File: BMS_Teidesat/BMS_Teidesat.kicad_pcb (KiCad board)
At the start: 2 copper layers, 90.2 x 95.9 mm, 10 parts

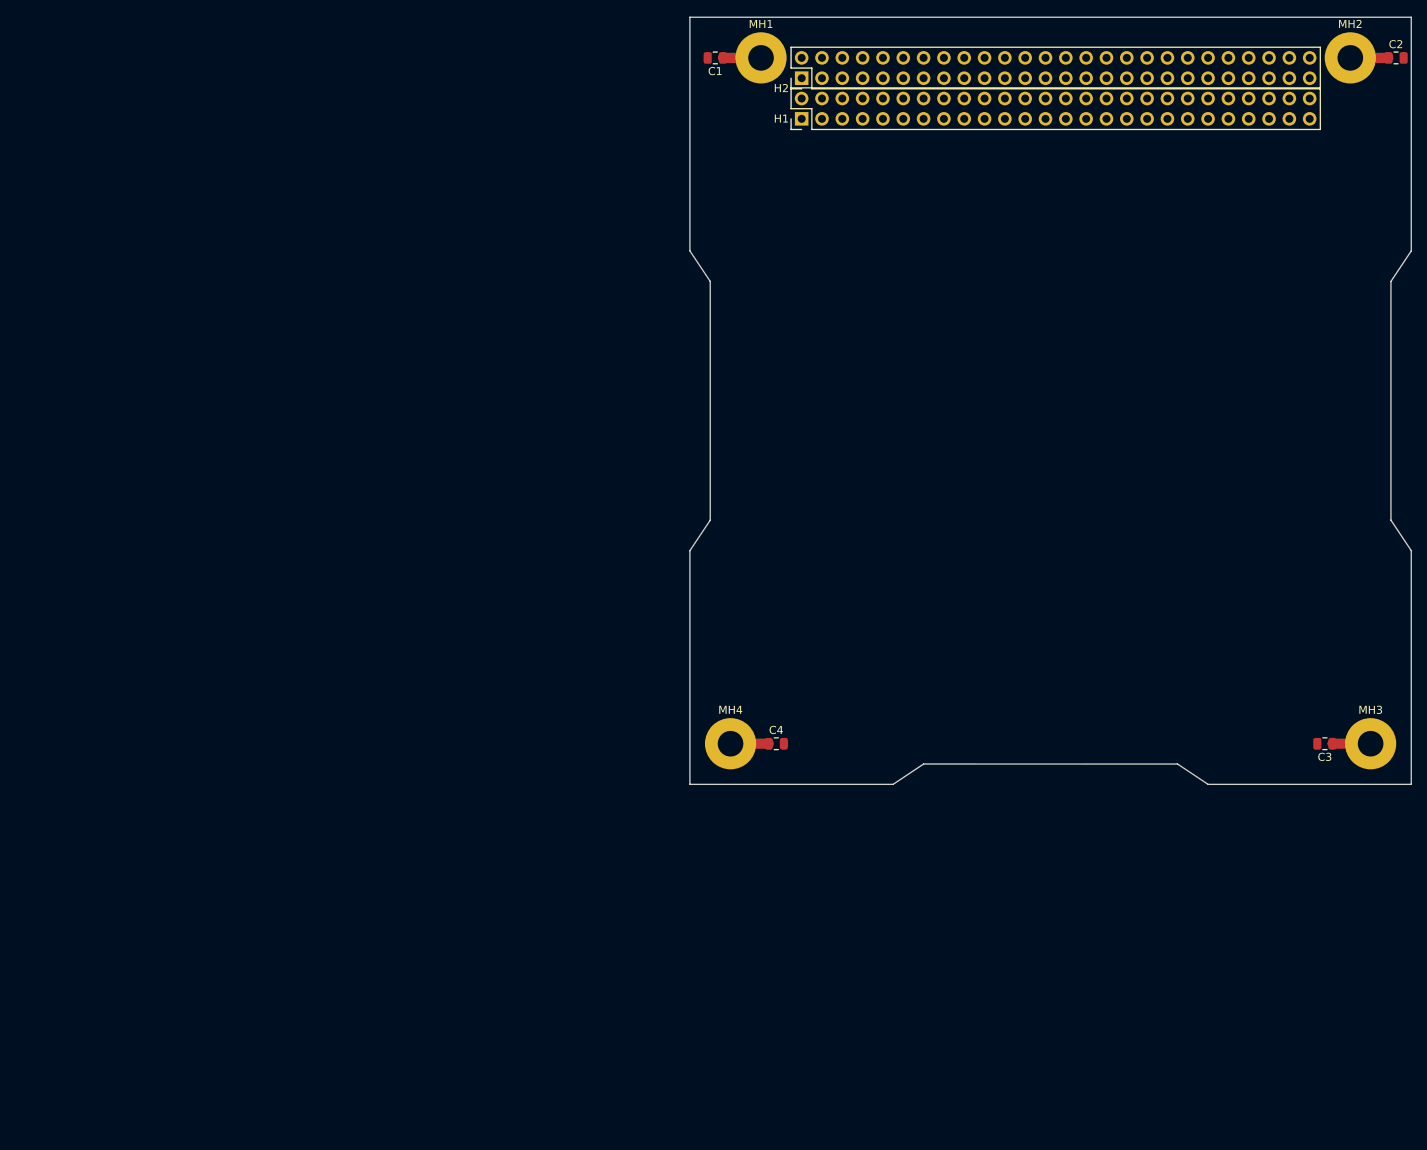
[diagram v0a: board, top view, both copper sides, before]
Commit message: Comienzo de enrutado
Co-Authored-By: hugohdezmo <238262256+hugohdezmo@users.noreply.github.com>
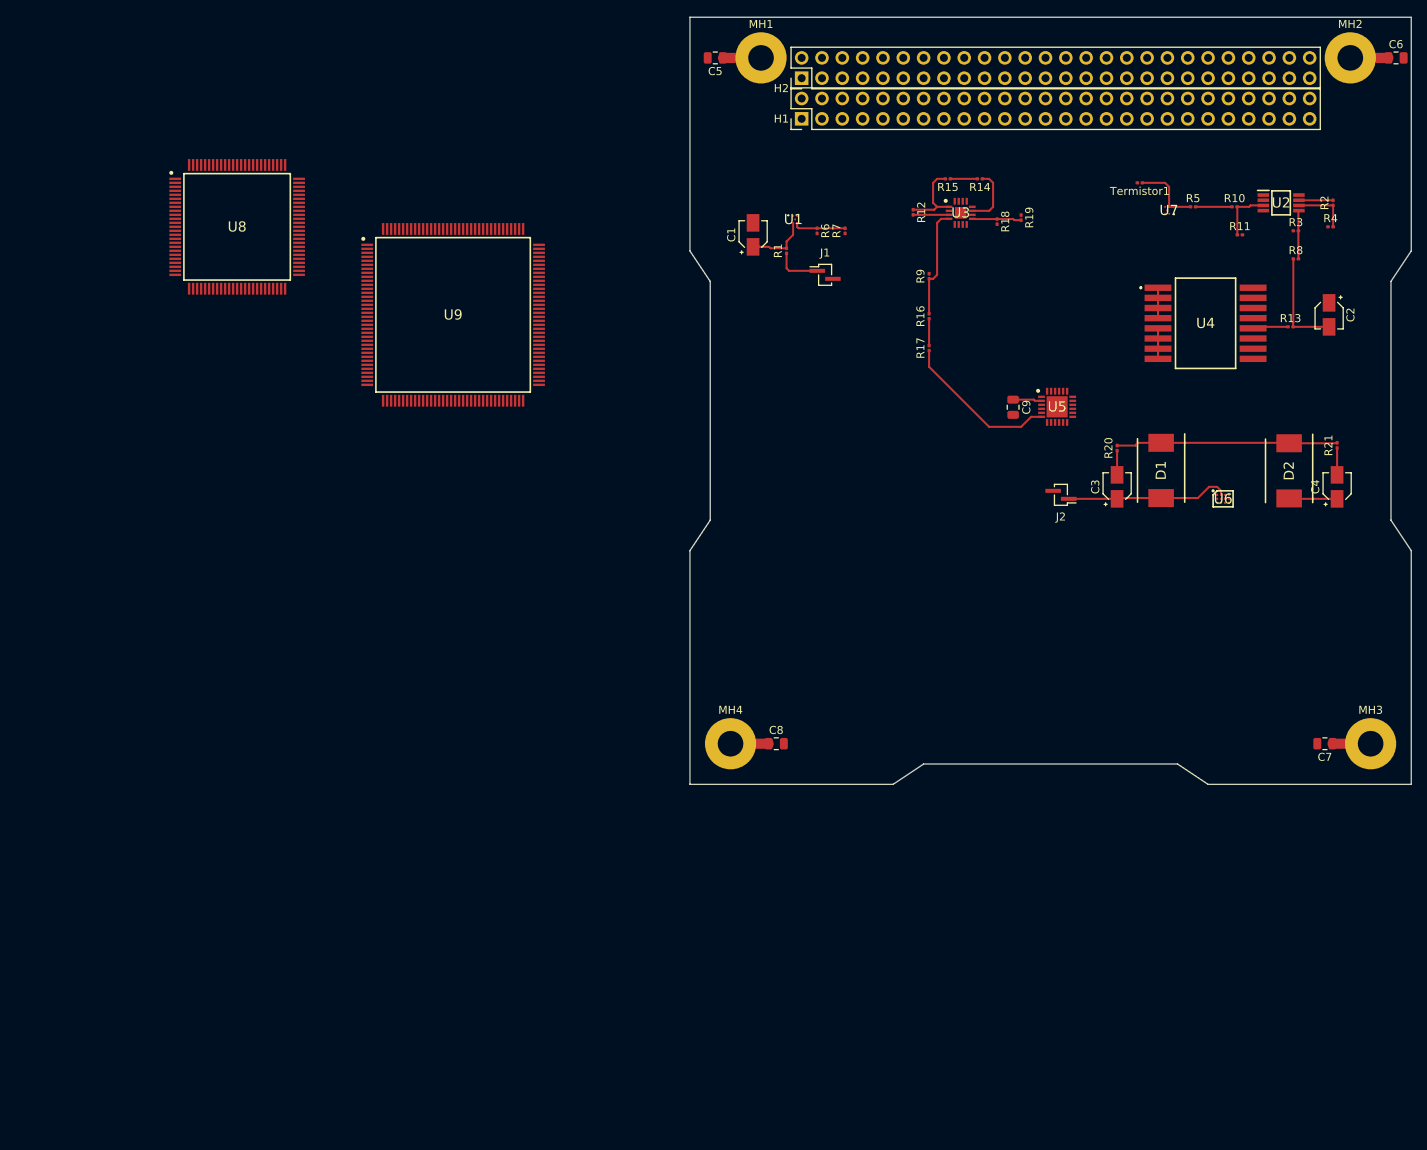
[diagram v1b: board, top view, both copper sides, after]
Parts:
- added C1: 1n, Capacitor_SMD:CP_Elec_3x5.3, F.Cu at (109.5, 78.0)
- added C2: 1n, Capacitor_SMD:CP_Elec_3x5.3, F.Cu at (181.5, 88.0)
- added C3: 10n, Capacitor_SMD:CP_Elec_3x5.3, F.Cu at (155.0, 109.5)
- added C4: 10n, Capacitor_SMD:CP_Elec_3x5.3, F.Cu at (182.5, 109.5)
- added C9: 10u, Capacitor_SMD:C_0805_2012Metric, F.Cu at (142.0, 99.5)
- added D1: SS14, Huellas BMS:DIOM8059X256N, F.Cu at (160.5, 107.5)
- added D2: SS14, Huellas BMS:DIOM8059X256N, F.Cu at (176.5, 107.5)
- added J1: Battery, Connector_PinSocket_1.00mm:PinSocket_1x02_P1.00mm_Vertical_SMD_Pin1Left, F.Cu at (118.5, 83.0)
- added J2: Battery, Connector_PinSocket_1.00mm:PinSocket_1x02_P1.00mm_Vertical_SMD_Pin1Left, F.Cu at (148.0, 110.5)
- added R1: 100, Resistor_SMD:R_0201_0603Metric, F.Cu at (113.7, 80.0)
- added R10: 40,2K, Resistor_SMD:R_0201_0603Metric, F.Cu at (169.7, 74.5)
- added R11: 10K, Resistor_SMD:R_0201_0603Metric, F.Cu at (170.3, 78.0)
- added R12: 1000, Resistor_SMD:R_0201_0603Metric, F.Cu at (129.5, 75.2)
- added R13: 100, Resistor_SMD:R_0201_0603Metric, F.Cu at (176.7, 89.5)
- added R14: 210, Resistor_SMD:R_0201_0603Metric, F.Cu at (137.8, 71.0)
- added R15: 1870, Resistor_SMD:R_0201_0603Metric, F.Cu at (133.8, 71.0)
- added R16: 1870, Resistor_SMD:R_0201_0603Metric, F.Cu at (131.5, 88.2)
- added R17: 210, Resistor_SMD:R_0201_0603Metric, F.Cu at (131.5, 92.2)
- added R18: 10K, Resistor_SMD:R_0201_0603Metric, F.Cu at (140.0, 76.3)
- added R19: 10K, Resistor_SMD:R_0201_0603Metric, F.Cu at (143.0, 75.8)
- added R2: 50,5K, Resistor_SMD:R_0201_0603Metric, F.Cu at (182.0, 74.0)
- added R20: 10, Resistor_SMD:R_0201_0603Metric, F.Cu at (155.0, 104.7)
- added R21: 10, Resistor_SMD:R_0201_0603Metric, F.Cu at (182.5, 104.3)
- added R3: 50,5k, Resistor_SMD:R_0201_0603Metric, F.Cu at (177.3, 77.5)
- added R4: 80,6K, Resistor_SMD:R_0201_0603Metric, F.Cu at (181.7, 77.0)
- added R5: 10k, Resistor_SMD:R_0201_0603Metric, F.Cu at (164.5, 74.5)
- added R6: 10K, Resistor_SMD:R_0201_0603Metric, F.Cu at (117.5, 77.5)
- added R7: 10K, Resistor_SMD:R_0201_0603Metric, F.Cu at (121.0, 77.5)
- added R8: 80,6K, Resistor_SMD:R_0201_0603Metric, F.Cu at (177.3, 81.0)
- added R9: 1000, Resistor_SMD:R_0201_0603Metric, F.Cu at (131.5, 83.2)
- added Termistor1: 10k, Resistor_SMD:R_0201_0603Metric, F.Cu at (157.8, 71.5)
- added U1: AD8605ACBZ-REEL7, Huellas BMS:AD8605ACBZREEL7, F.Cu at (114.8, 76.1)
- added U2: AD8606ARMZ-REEL, Huellas BMS:SOP65P490X110-8N, F.Cu at (175.5, 74.0)
- added U3: ADA4940-1ACPZ-R7, Huellas BMS:QFN50P300X300X80-17N-D, F.Cu at (135.4, 75.2)
- added U4: ACS37002LMCATR-050B5, Huellas BMS:ACS37002LMCA050U5, F.Cu at (166.1, 89.1)
- added U5: AD7091R-8BCPZ-RL7, Huellas BMS:QFN50P400X400X80-25N-D, F.Cu at (147.5, 99.5)
- added U6: CSD86311W1723, Huellas BMS:BGA12C50P4X3_228X170X62, F.Cu at (168.2, 111.0)
- added U7: AD8605ACBZ-REEL7, Huellas BMS:AD8605ACBZREEL7, F.Cu at (161.2, 74.9)
- added U8: STM32G474VET6, Huellas BMS:QFP50P1600X1600X160-100N, F.Cu at (45.0, 77.0)
- added U9: TMS5703137DPGEQQ1, Huellas BMS:QFP50P2200X2200X160-144N, F.Cu at (72.0, 88.0)
- renumbered C1 to C5, C2 to C6, C3 to C7, C4 to C8
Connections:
- H1 pad 11: TX2/GP8 -> unconnected-(H1-Pin_11-Pad11)
- H1 pad 13: GP15/A1/RX3 -> unconnected-(H1-Pin_13-Pad13)
- H1 pad 17: GP21/A7/RX5 -> unconnected-(H1-Pin_17-Pad17)
- H1 pad 46: CS/GP10 -> unconnected-(H1-Pin_46-Pad46)
- H1 pad 48: CS/GP37 -> unconnected-(H1-Pin_48-Pad48)
- H1 pad 50: CS/GP36 -> unconnected-(H1-Pin_50-Pad50)
- H1 pad 7: TX1/GP1 -> unconnected-(H1-Pin_7-Pad7)
- H1 pad 9: RX2/GP7 -> unconnected-(H1-Pin_9-Pad9)
- H2 pad 10: SW2 -> unconnected-(H2-Pin_10-Pad10)
- H2 pad 11: SW3 -> unconnected-(H2-Pin_11-Pad11)
- H2 pad 12: SW4 -> unconnected-(H2-Pin_12-Pad12)
- H2 pad 13: SW5 -> unconnected-(H2-Pin_13-Pad13)
- H2 pad 14: SW6 -> unconnected-(H2-Pin_14-Pad14)
- H2 pad 15: SW7 -> unconnected-(H2-Pin_15-Pad15)
- H2 pad 16: SW8 -> unconnected-(H2-Pin_16-Pad16)
- H2 pad 17: SW9 -> unconnected-(H2-Pin_17-Pad17)
- H2 pad 18: SW10 -> unconnected-(H2-Pin_18-Pad18)
- H2 pad 19: SW11 -> unconnected-(H2-Pin_19-Pad19)
- H2 pad 20: SW12 -> unconnected-(H2-Pin_20-Pad20)
- H2 pad 21: unconnected-(H2-Pad21) -> GND
- H2 pad 22: unconnected-(H2-Pad22) -> GND
- H2 pad 25: unconnected-(H2-Pad25) -> +5V
- H2 pad 26: unconnected-(H2-Pad26) -> +5V
- H2 pad 27: unconnected-(H2-Pad27) -> +3V3
- H2 pad 28: unconnected-(H2-Pad28) -> +3V3
- H2 pad 29: unconnected-(H2-Pad29) -> GND
- H2 pad 30: unconnected-(H2-Pad30) -> GND
- H2 pad 31: unconnected-(H2-Pad31) -> GND
- H2 pad 32: unconnected-(H2-Pad32) -> GND
- H2 pad 35: PCM_IN -> unconnected-(H2-Pin_35-Pad35)
- H2 pad 41: BCR_OUT -> unconnected-(H2-Pin_41-Pad41)
- H2 pad 43: BCR_OUT -> unconnected-(H2-Pin_43-Pad43)
- H2 pad 44: BCR_OUT -> unconnected-(H2-Pin_44-Pad44)
- H2 pad 45: unconnected-(H2-Pad45) -> +BATT
- H2 pad 46: unconnected-(H2-Pad46) -> +BATT
- H2 pad 9: SW1 -> unconnected-(H2-Pin_9-Pad9)
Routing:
- net /+BATTERY: track 0.00 -> 31.6 mm
- net Net-(D1-A): track 0.00 -> 20.4 mm
- net /+VBAT: track 0.00 -> 19.7 mm
- net Net-(U3-+FB): track 0.00 -> 13.8 mm
- net Net-(C2-Pad2): track 0.00 -> 13.0 mm
- net Net-(U3--FB): track 0.00 -> 9.59 mm
- net Net-(U7-+IN): track 0.00 -> 8.72 mm
- net Net-(U1-+IN): track 0.00 -> 7.77 mm
- net /-VBAT: track 0.00 -> 7.35 mm
- net Net-(U2--IN_B): track 0.00 -> 6.96 mm
- net Net-(U2-+IN_A): track 0.00 -> 6.86 mm
- net Net-(U1--IN): track 0.00 -> 6.57 mm
- net /VOCM1: track 0.00 -> 6.19 mm
- net Net-(U2-+IN_B): track 0.00 -> 6.05 mm
- net /EPS: track 0.00 -> 6.02 mm
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
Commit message: Se ha hecho un primer conexionado de la PCB
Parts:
- moved U9 95.0 mm to (167.0, 89.0)
- moved R4 60.9 mm to (134.5, 115.5)
- moved C2 59.4 mm to (131.5, 120.0), turned to 180 degrees
- moved R10 58.4 mm to (122.7, 109.1)
- moved R11 58.4 mm to (123.3, 112.6)
- moved R13 58.4 mm to (129.7, 124.1)
- moved R2 58.4 mm to (135.0, 108.6)
- moved R3 58.4 mm to (130.3, 112.1)
- moved R5 58.4 mm to (117.5, 109.1)
- moved R8 58.4 mm to (130.3, 115.6)
- moved U2 58.4 mm to (128.5, 108.6)
- moved U7 58.4 mm to (114.2, 109.6)
- moved U4 58.4 mm to (119.1, 123.7)
- moved Termistor1 53.6 mm to (168.5, 124.0), turned to 0 degrees
- moved J2 20.3 mm to (153.5, 130.0)
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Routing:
- net /TEMP: track 0.00 -> 154.5 mm
- net /+BATTERY: track 31.6 -> 125.1 mm
- net /REFOUT: track 4.54 -> 86.9 mm
- net Net-(U7-+IN): track 8.72 -> 81.8 mm
- net /+LOAD: track 3.81 -> 64.2 mm
- net Net-(U2--IN_A): track 0.00 -> 51.0 mm
- net Net-(U1-OUT): track 0.00 -> 28.6 mm
- net /CONTROL2: track 0.00 -> 27.0 mm
- net /CONTROL1: track 0.00 -> 26.0 mm
- net /+VBAT: track 19.7 -> 42.3 mm
- net /OUT CAD: track 0.00 -> 16.0 mm
- net /+HALL: track 4.28 -> 19.6 mm
- net /CLOCK MC: track 0.00 -> 15.0 mm
- net /GIOA: track 0.00 -> 14.0 mm
- net /CS: track 0.00 -> 12.8 mm
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
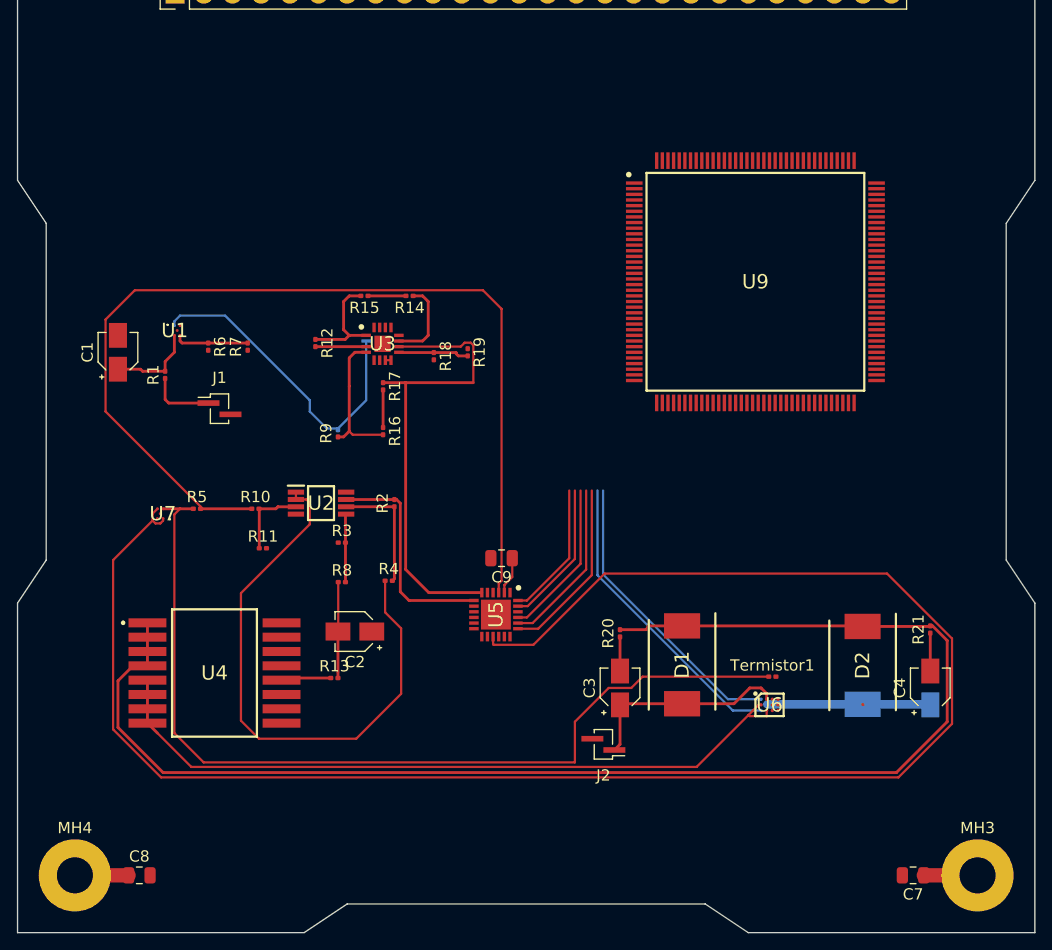
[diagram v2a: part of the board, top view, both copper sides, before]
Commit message: Se ha corregido el enrutado de la PCB. Faltan las conexiones de alimentación y de tierra
Co-Authored-By: Angel-Castro-Vega <236372966+Angel-Castro-Vega@users.noreply.github.com>
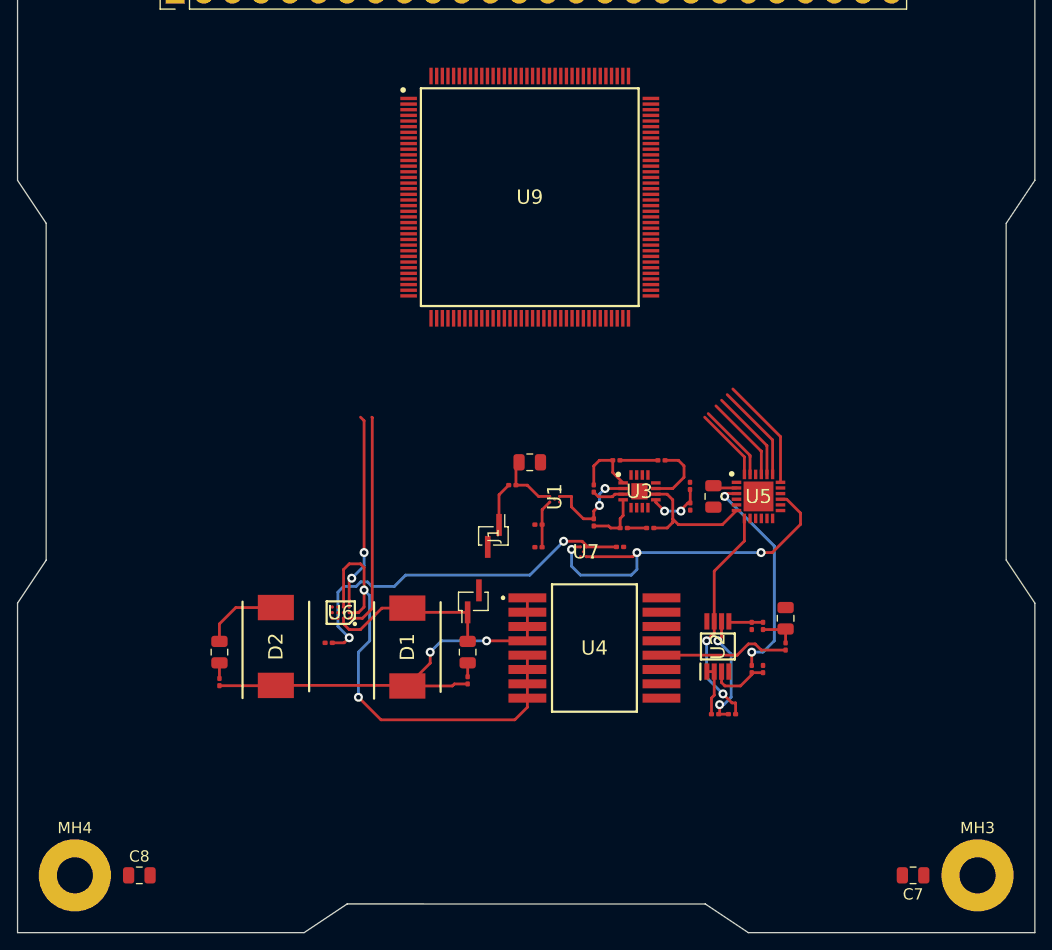
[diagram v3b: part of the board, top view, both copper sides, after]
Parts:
- C1, C2, C3, C4: footprint Capacitor_SMD:CP_Elec_3x5.3 -> Capacitor_SMD:C_0805_2012Metric
- moved R21 63.2 mm to (119.5, 124.5), turned to -90 degrees
- moved C4 63.1 mm to (119.5, 121.8), turned to -90 degrees
- moved D2 52.0 mm to (124.5, 121.3), turned to 90 degrees
- moved R10 46.2 mm to (166.7, 123.3), turned to -90 degrees
- moved R11 45.6 mm to (167.7, 123.3), turned to 90 degrees
- moved R13 40.1 mm to (169.7, 121.3), turned to 90 degrees
- moved Termistor1 39.4 mm to (129.2, 121.0), turned to 180 degrees
- moved U6 38.9 mm to (130.2, 118.3), turned to 180 degrees
- moved C2 38.2 mm to (169.7, 118.8), turned to -90 degrees
- moved C1 37.8 mm to (147.0, 105.0), turned to 0 degrees
- moved R5 37.7 mm to (155.0, 112.5)
- moved U7 37.7 mm to (151.8, 112.9)
- moved R8 37.5 mm to (167.7, 119.5), turned to 90 degrees
- moved U2 37.4 mm to (163.7, 121.3), turned to 90 degrees
- moved R3 37.1 mm to (166.7, 119.5), turned to 90 degrees
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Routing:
- net /TEMP: track 154.5 -> 33.7 mm, vias 0 -> 3
- net /+BATTERY: track 125.1 -> 40.1 mm, vias 0 -> 2
- net /REFOUT: track 86.9 -> 19.4 mm, vias 0 -> 2
- net Net-(U7-+IN): track 81.8 -> 33.3 mm, vias 0 -> 2
- net Net-(U2--IN_A): track 51.0 -> 4.53 mm
- net /+VBAT: track 42.3 -> 12.0 mm
- net /+LOAD: track 64.2 -> 41.5 mm, vias 0 -> 2
- net Net-(U1-OUT): track 28.6 -> 9.09 mm, vias 0 -> 2
- net /MOSI MC: track 0.00 -> 10.0 mm
- net /CONTROL2: track 27.0 -> 17.5 mm, vias 0 -> 2
- net Net-(U3-+FB): track 12.5 -> 5.02 mm
- net /EPS: track 14.6 -> 7.15 mm
- net /OUT CAD: track 16.0 -> 8.74 mm
- net Net-(U4-VIOUT): track 4.44 -> 11.6 mm
- net /CLOCK MC: track 15.0 -> 8.24 mm
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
